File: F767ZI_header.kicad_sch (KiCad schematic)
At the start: 19 parts, among them J1 I2C1_MD, J2 CAN1, J3 CAN2, J4 UART, J5 PowerBoard, J6 EMERSW_CON, J7 Encoder1, J8 Encoder2, J9 RESET_SW, SW1 SW_Push, U1 MCP2562-E-P, U2 MCP2562-E-P

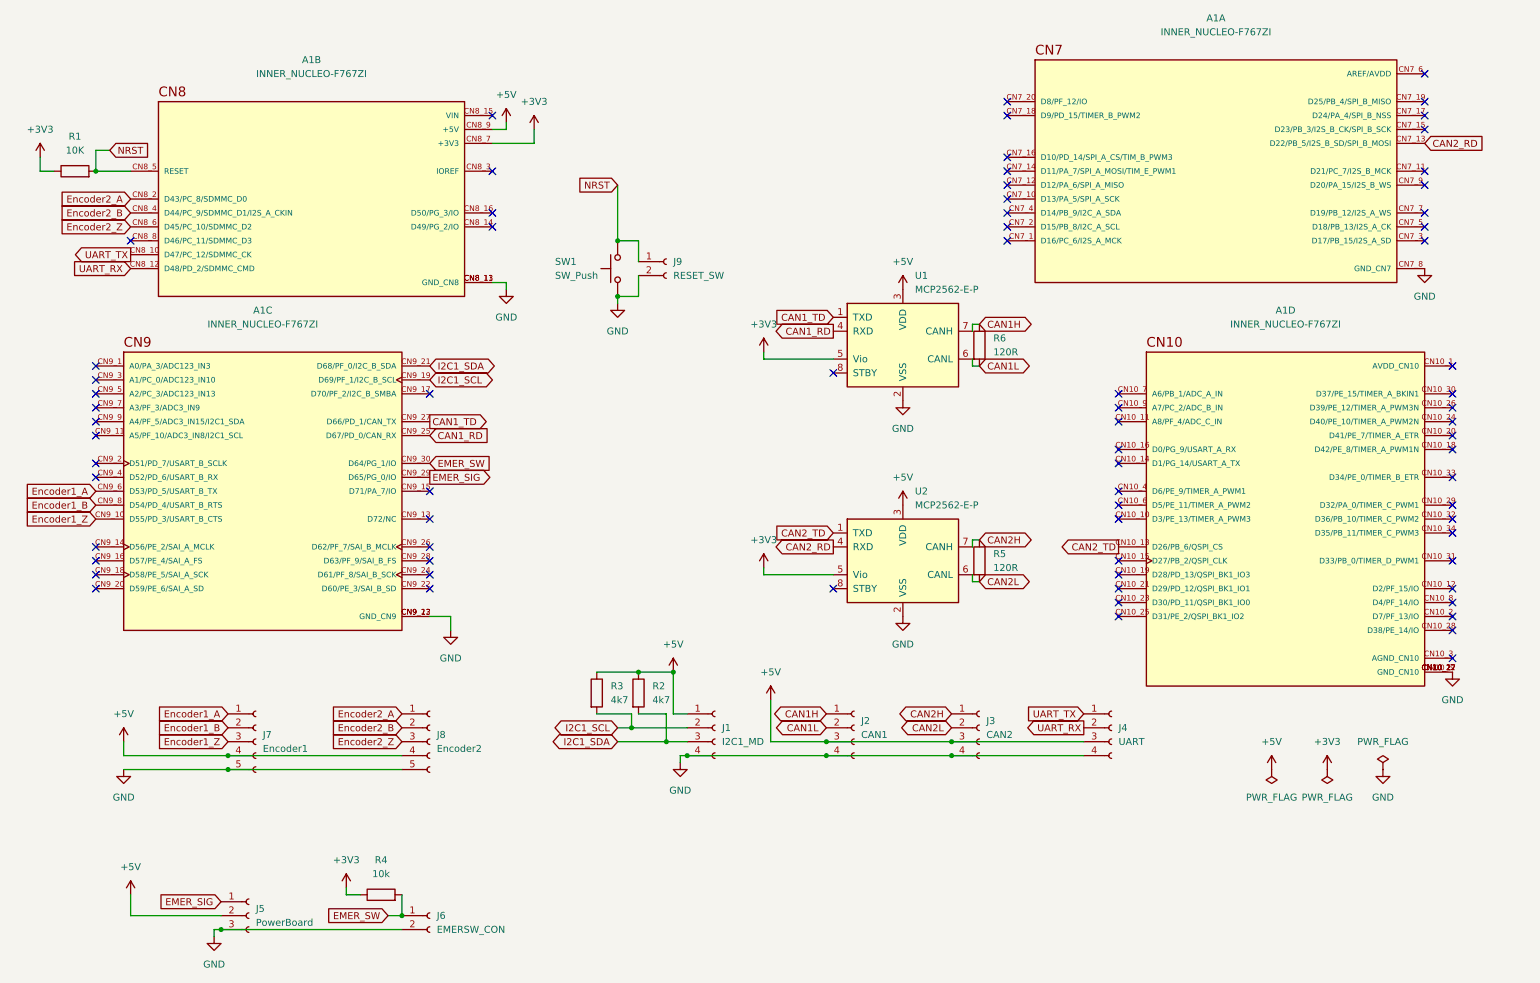
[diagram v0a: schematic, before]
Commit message: sch: Add a CAN connector
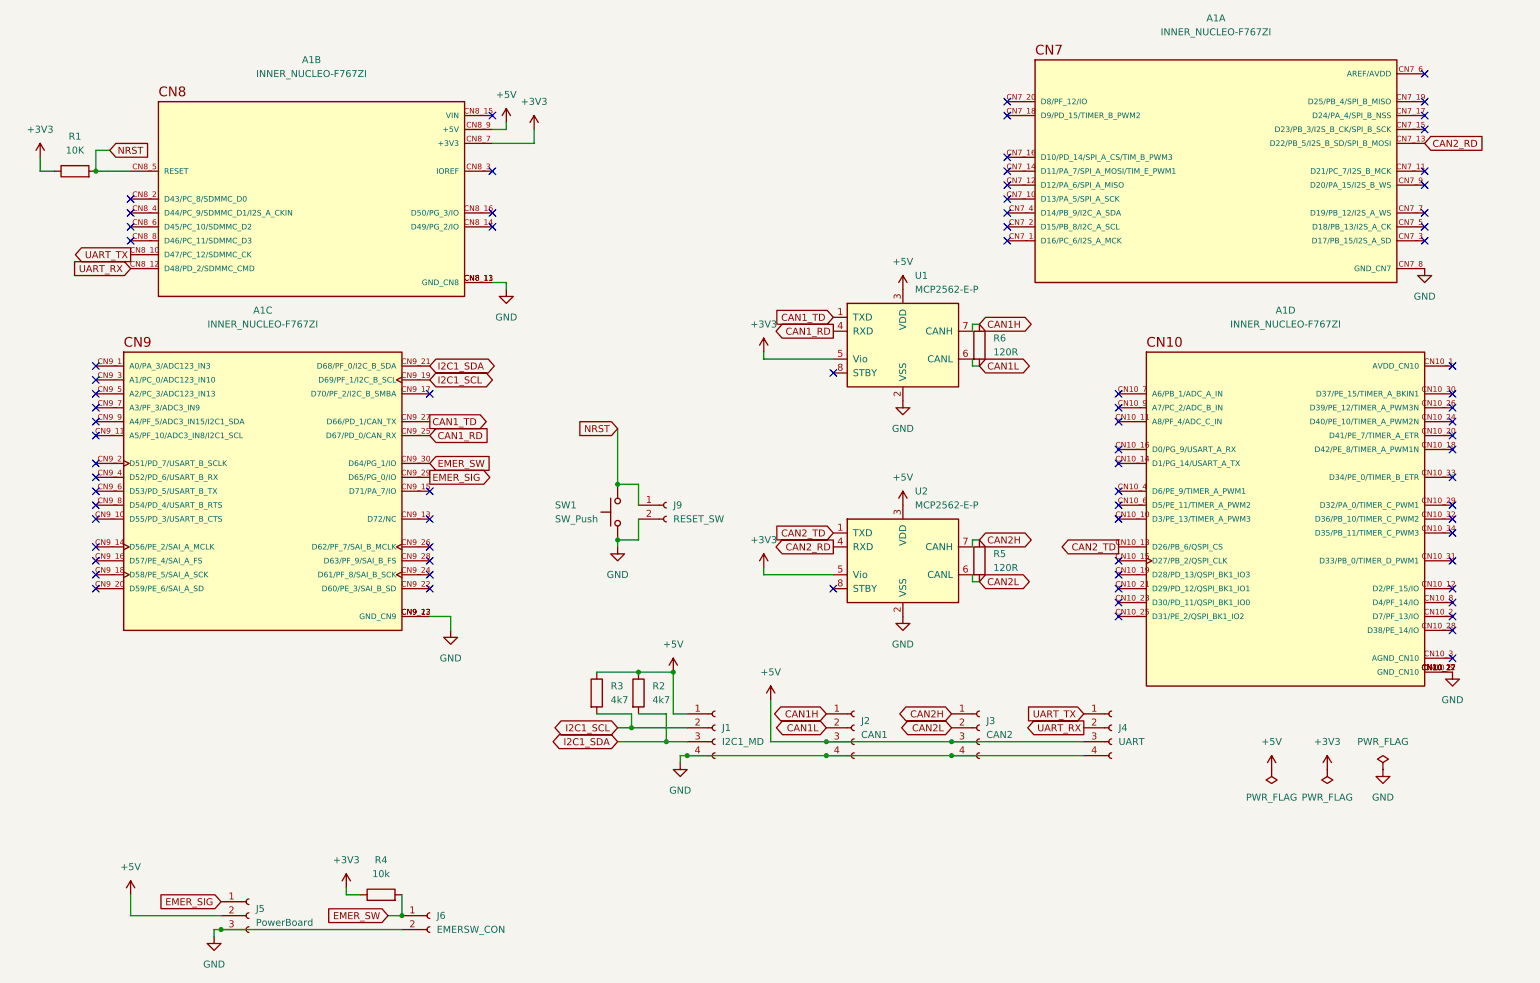
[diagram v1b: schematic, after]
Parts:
- removed J7: Encoder1, Connector_JST:JST_XA_B05B-XASK-1_1x05_P2.50mm_Vertical, symbol Connector:Conn_01x05_Socket
- removed J8: Encoder2, Connector_JST:JST_XA_B05B-XASK-1_1x05_P2.50mm_Vertical, symbol Connector:Conn_01x05_Socket
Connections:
- net Encoder1_A: no longer names the net of A1.CN9_6 (D53/PD_5/USART_B_TX)
- net Encoder1_B: no longer names the net of A1.CN9_8 (D54/PD_4/USART_B_RTS)
- net Encoder1_Z: no longer names the net of A1.CN9_10 (D55/PD_3/USART_B_CTS)
- net Encoder2_A: no longer names the net of A1.CN8_2 (D43/PC_8/SDMMC_D0)
- net Encoder2_B: no longer names the net of A1.CN8_4 (D44/PC_9/SDMMC_D1/I2S_A_CKIN)
- net Encoder2_Z: no longer names the net of A1.CN8_6 (D45/PC_10/SDMMC_D2)
- no-connect marks 73 -> 79
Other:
- moved on the sheet: J9, SW1

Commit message: SCH: add an I2C to use IMU & add C around MCP2562
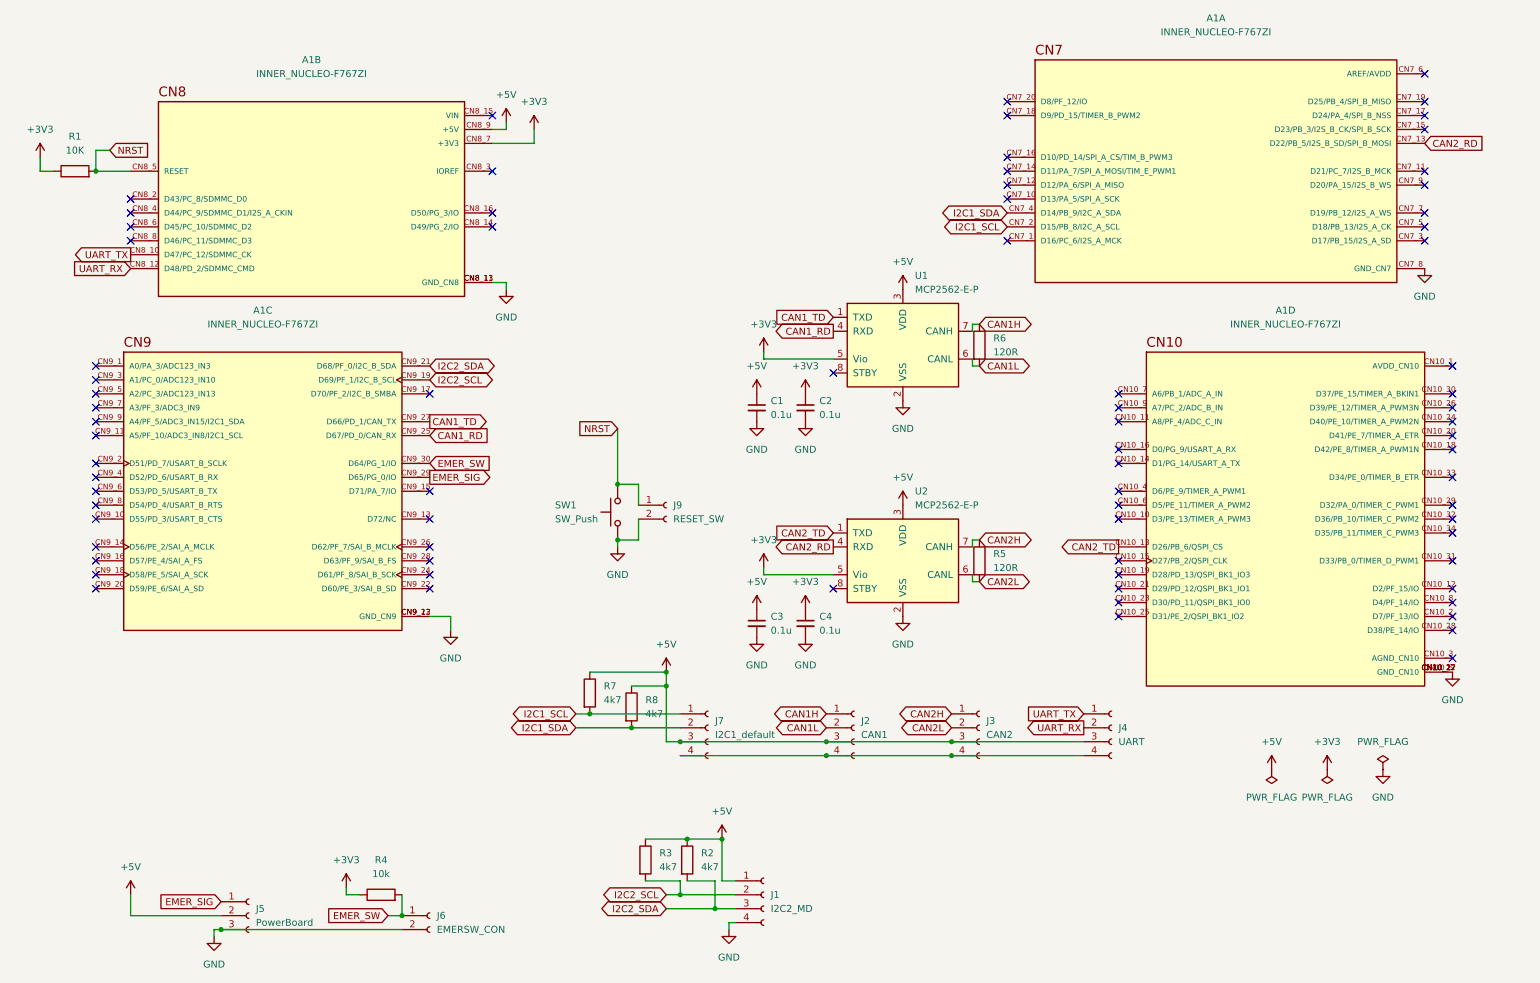
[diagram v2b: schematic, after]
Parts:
- added C1, C2, C3, C4: 0.1u, symbol Device:C_Small
- added J7: I2C1_default, symbol Connector:Conn_01x04_Socket
- added R7, R8: 4k7, Resistor_THT:R_Axial_DIN0207_L6.3mm_D2.5mm_P7.62mm_Horizontal, symbol Device:R
- J1: value I2C1_MD -> I2C2_MD
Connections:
- net +3V3: now also C2.1, C4.1
- net +5V: now also C1.1, C3.1, J7.3 (Pin_3), R7.1, R8.1
- net GND: now also C1.2, C2.2, C3.2, C4.2; no longer J2.4 (Pin_4), J3.4 (Pin_4), J4.4 (Pin_4)
- net I2C1_SCL: now also A1.CN7_2 (D15/PB_8/I2C_A_SCL), J7.1 (Pin_1), R7.2; no longer A1.CN9_19 (D69/PF_1/I2C_B_SCL), J1.2 (Pin_2), R3.2
- net I2C1_SDA: now also A1.CN7_4 (D14/PB_9/I2C_A_SDA), J7.2 (Pin_2), R8.2; no longer A1.CN9_21 (D68/PF_0/I2C_B_SDA), J1.3 (Pin_3), R2.2
- new net: J2.4 (Pin_4), J3.4 (Pin_4), J4.4 (Pin_4), J7.4 (Pin_4)
- new net I2C2_SCL: A1.CN9_19 (D69/PF_1/I2C_B_SCL), J1.2 (Pin_2), R3.2
- new net I2C2_SDA: A1.CN9_21 (D68/PF_0/I2C_B_SDA), J1.3 (Pin_3), R2.2
- no-connect marks 79 -> 77
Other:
- moved on the sheet: J1, R2, R3

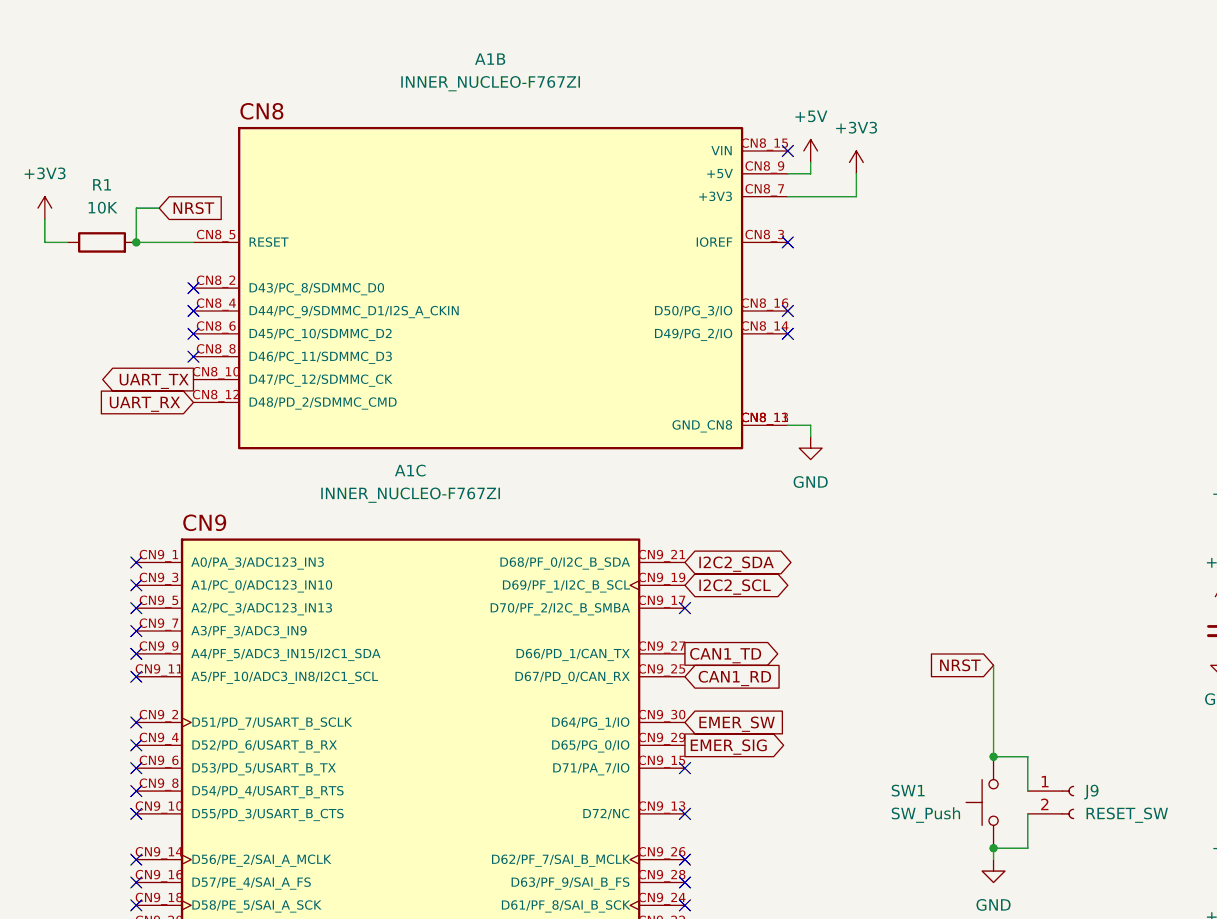
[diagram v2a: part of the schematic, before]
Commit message: SCH: Replace pull-up of NRST
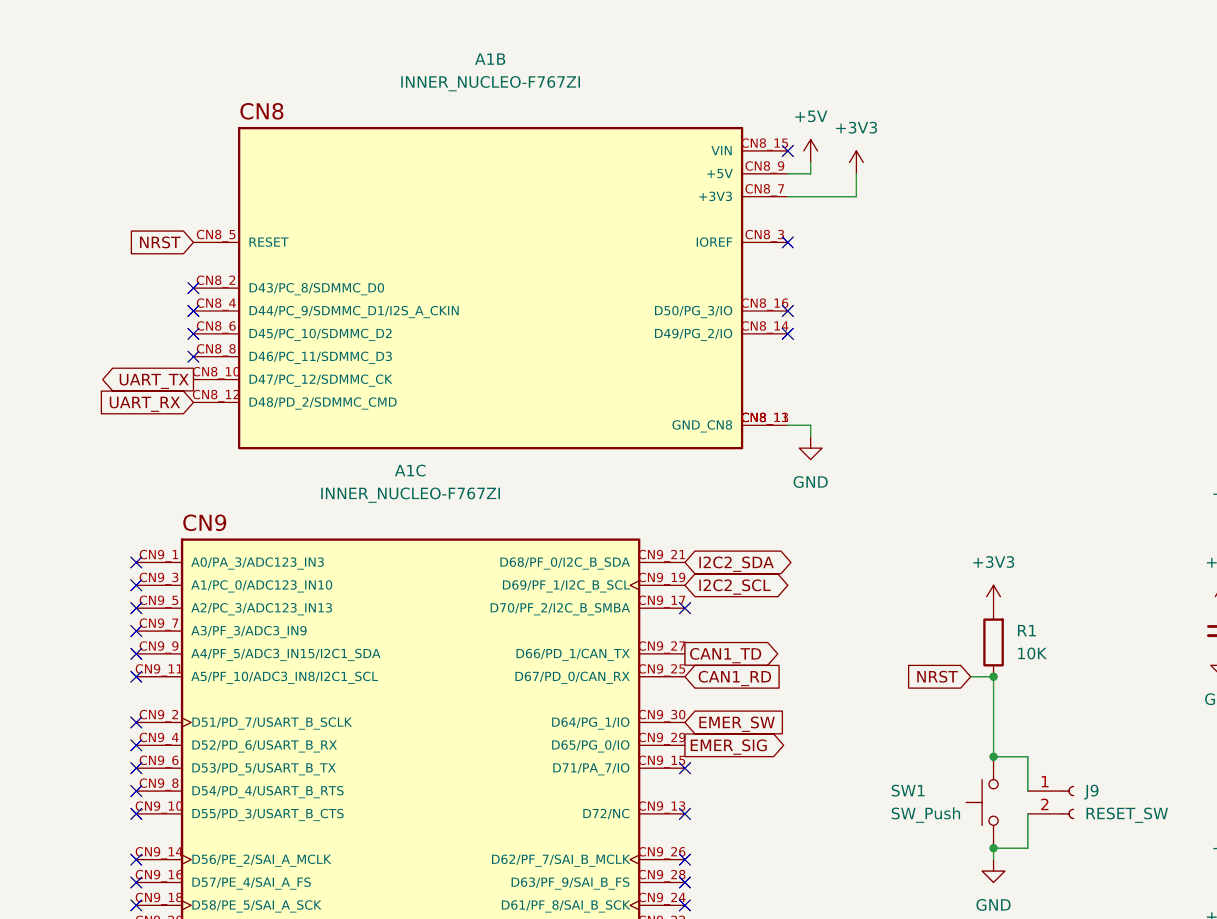
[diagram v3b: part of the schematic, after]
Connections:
- net +3V3: now also R1.2; no longer R1.1
- net NRST: now also R1.1; no longer R1.2
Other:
- moved on the sheet: R1
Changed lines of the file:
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@@
 	)
 	(junction
-		(at 182.88 152.4)
+		(at 121.92 96.52)
 		(diameter 0)
 		(color 0 0 0 0)
 	)
 	(junction
-		(at 116.84 147.32)
+		(at 182.88 152.4)
 		(diameter 0)
 		(color 0 0 0 0)
 	)
 	(junction
-		(at 26.67 48.26)
+		(at 116.84 147.32)
 		(diameter 0)
 		(color 0 0 0 0)
@@
 	(wire
 		(pts
+			(xy 119.38 96.52) (xy 121.92 96.52)
+		)
+		(stroke
+			(width 0)
+			(type default)
+		)
+	)
+	(wire
+		(pts
 			(xy 130.81 152.4) (xy 133.35 152.4)
 		)
@@
 	(wire
 		(pts
+			(xy 121.92 96.52) (xy 121.92 105.41)
+		)
+		(stroke
+			(width 0)
+			(type default)
+		)
+	)
+	(wire
+		(pts
 			(xy 182.88 154.94) (xy 207.01 154.94)
 		)
@@
 	(wire
 		(pts
-			(xy 26.67 48.26) (xy 33.02 48.26)
-		)
-		(stroke
-			(width 0)
-			(type default)
-		)
-	)
-	(wire
-		(pts
 			(xy 125.73 109.22) (xy 125.73 105.41)
 		)
@@
 	(wire
 		(pts
-			(xy 29.21 44.45) (xy 26.67 44.45)
-		)
-		(stroke
-			(width 0)
-			(type default)
-		)
-	)
-	(wire
-		(pts
 			(xy 142.24 185.42) (xy 143.51 185.42)
 		)
@@
 	(wire
 		(pts
-			(xy 16.51 45.72) (xy 16.51 48.26)
-		)
-		(stroke
-			(width 0)
-			(type default)
-		)
-	)
-	(wire
-		(pts
 			(xy 160.02 152.4) (xy 182.88 152.4)
 		)
@@
 	(wire
 		(pts
-			(xy 16.51 48.26) (xy 19.05 48.26)
-		)
-		(stroke
-			(width 0)
-			(type default)
-		)
-	)
-	(wire
-		(pts
 			(xy 48.26 187.96) (xy 48.26 186.69)
 		)
@@
 	(wire
 		(pts
-			(xy 26.67 44.45) (xy 26.67 48.26)
-		)
-		(stroke
-			(width 0)
-			(type default)
-		)
-	)
-	(wire
-		(pts
-			(xy 121.92 95.25) (xy 121.92 105.41)
-		)
-		(stroke
-			(width 0)
-			(type default)
-		)
-	)
-	(wire
-		(pts
 			(xy 72.39 179.07) (xy 72.39 180.34)
 		)
@@
 	(global_label "NRST"
 		(shape input)
-		(at 29.21 44.45 0)
+		(at 33.02 48.26 180)
 		(fields_autoplaced yes)
 		(effects
@@
 				(size 1.27 1.27)
 			)
-			(justify left)
+			(justify right)
 		)
 		(property "Intersheetrefs" "${INTERSHEET_REFS}"
-			(at 36.9728 44.45 0)
+			(at 25.2572 48.26 0)
 			(effects
 				(font
 					(size 1.27 1.27)
 				)
-				(justify left)
+				(justify right)
 				(hide yes)
 			)
@@
 	(global_label "NRST"
 		(shape input)
-		(at 121.92 95.25 180)
+		(at 119.38 96.52 180)
 		(fields_autoplaced yes)
 		(effects
@@
 		)
 		(property "Intersheetrefs" "${INTERSHEET_REFS}"
-			(at 114.1572 95.25 0)
+			(at 111.6172 96.52 0)
 			(effects
 				(font
@@
 	(symbol
 		(lib_id "Device:R")
-		(at 22.86 48.26 90)
+		(at 121.92 92.71 180)
 		(unit 1)
 		(exclude_from_sim no)
@@
 		(fields_autoplaced yes)
 		(property "Reference" "R1"
-			(at 22.86 41.91 90)
+			(at 124.46 91.4399 0)
 			(effects
 				(font
 					(size 1.27 1.27)
 				)
+				(justify right)
 			)
 		)
 		(property "Value" "10K"
-			(at 22.86 44.45 90)
+			(at 124.46 93.9799 0)
 			(effects
 				(font
 					(size 1.27 1.27)
 				)
+				(justify right)
 			)
 		)
 		(property "Footprint" "Resistor_THT:R_Axial_DIN0207_L6.3mm_D2.5mm_P7.62mm_Horizontal"
-			(at 22.86 50.038 90)
+			(at 123.698 92.71 90)
 			(effects
 				(font
@@
 		)
 		(property "Datasheet" "~"
-			(at 22.86 48.26 0)
+			(at 121.92 92.71 0)
 			(effects
 				(font
@@
 		)
 		(property "Description" "Resistor"
-			(at 22.86 48.26 0)
+			(at 121.92 92.71 0)
 			(effects
 				(font
@@
 	(symbol
 		(lib_id "power:+3V3")
-		(at 16.51 45.72 0)
+		(at 121.92 88.9 0)
 		(unit 1)
 		(exclude_from_sim no)
@@
 		(fields_autoplaced yes)
 		(property "Reference" "#PWR08"
-			(at 16.51 49.53 0)
+			(at 121.92 92.71 0)
 			(effects
 				(font
@@
 		)
 		(property "Value" "+3V3"
-			(at 16.51 40.64 0)
+			(at 121.92 83.82 0)
 			(effects
 				(font
@@
 		)
 		(property "Footprint" ""
-			(at 16.51 45.72 0)
+			(at 121.92 88.9 0)
 			(effects
 				(font
@@
 		)
 		(property "Datasheet" ""
-			(at 16.51 45.72 0)
+			(at 121.92 88.9 0)
 			(effects
 				(font
@@
 		)
 		(property "Description" "Power symbol creates a global label with name \"+3V3\""
-			(at 16.51 45.72 0)
+			(at 121.92 88.9 0)
 			(effects
 				(font
